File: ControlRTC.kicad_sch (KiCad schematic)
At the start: 40 parts, among them M1 Fan_4pin, SW1 SW_USER, SW2 SW_WIPE, U18 74LVC1G07, U19 74LVC1G07, U20 LP5569RTWR, U21 PCF85063AT, U25 PCF8563TS, U27 74LVC1G07, Y2 32768Hz{slash}12.5pF

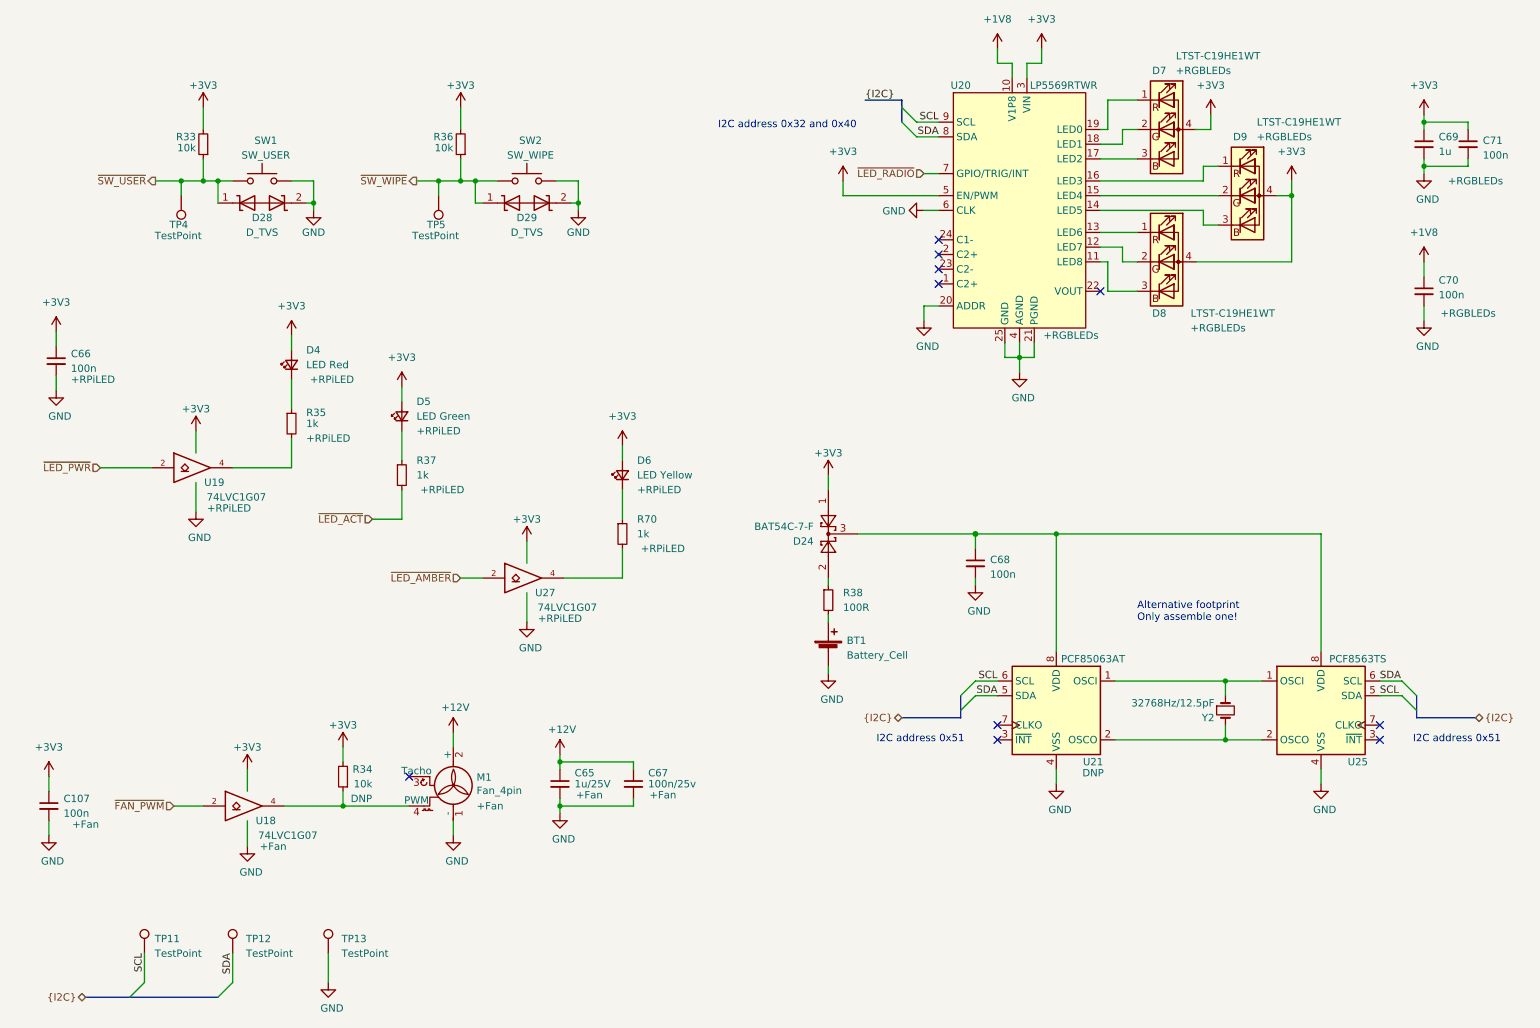
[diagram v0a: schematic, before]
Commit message: Yellow Proto1
Changes:
-name changed to yellow
-moved to 24-pin CP2102N
-routing

Signed-off-by: Dominik Sliwa <dominik@sliwa.io>
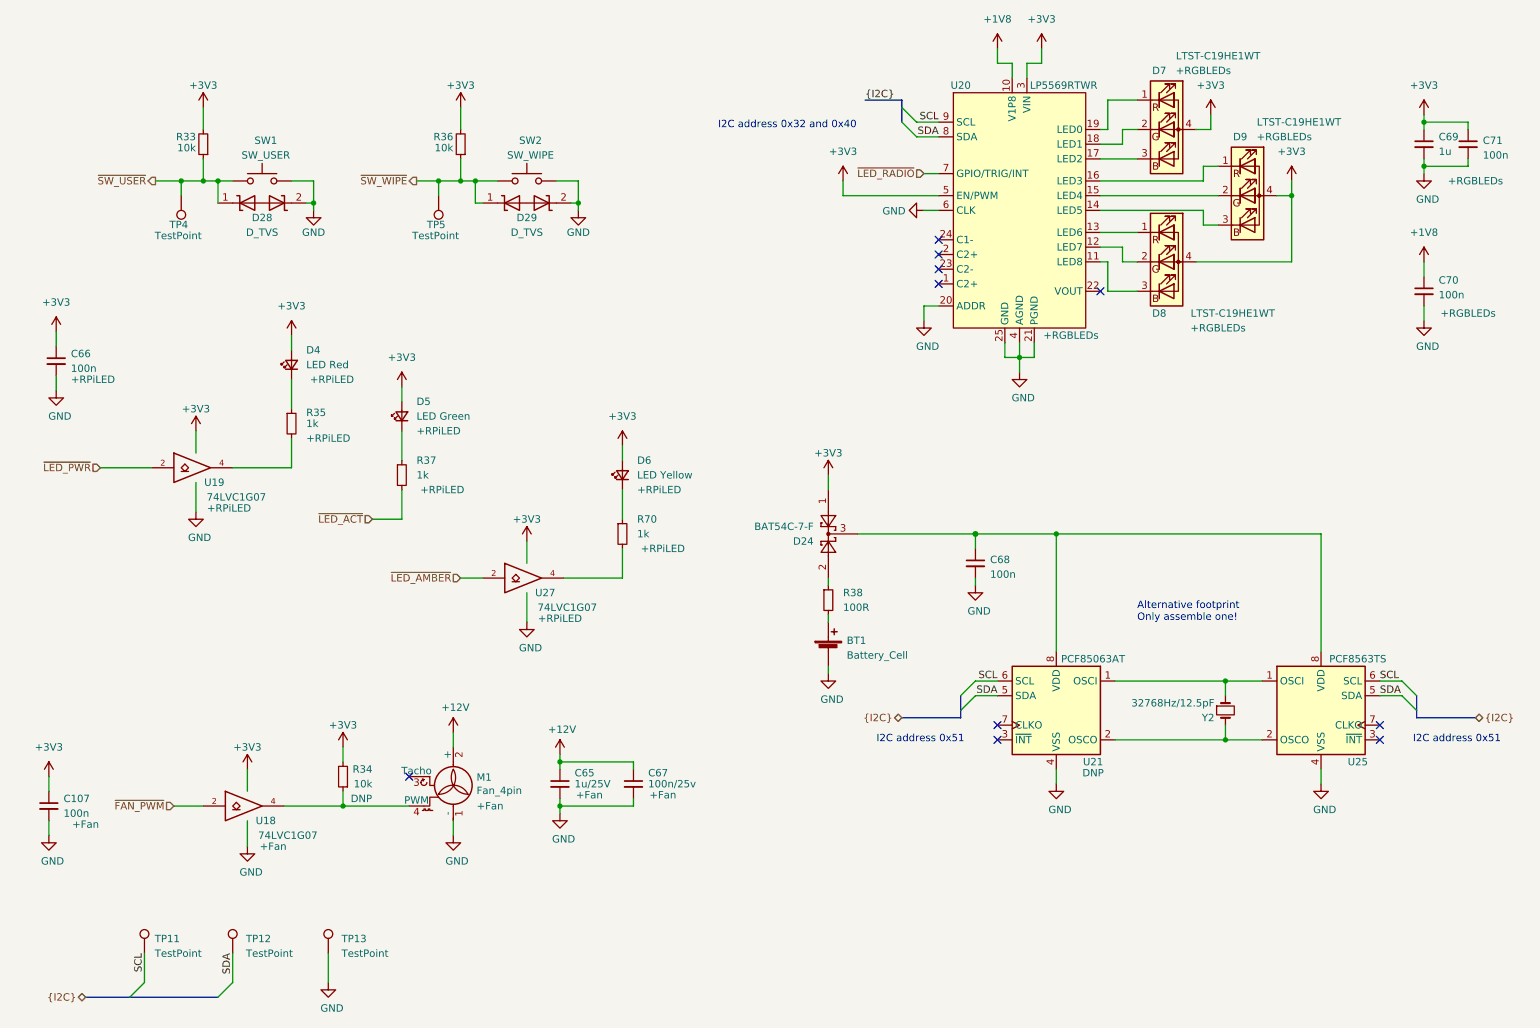
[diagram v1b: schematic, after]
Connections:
- net SCL: now also U25.6 (SCL); no longer U25.5 (SDA)
- net SDA: now also U25.5 (SDA); no longer U25.6 (SCL)

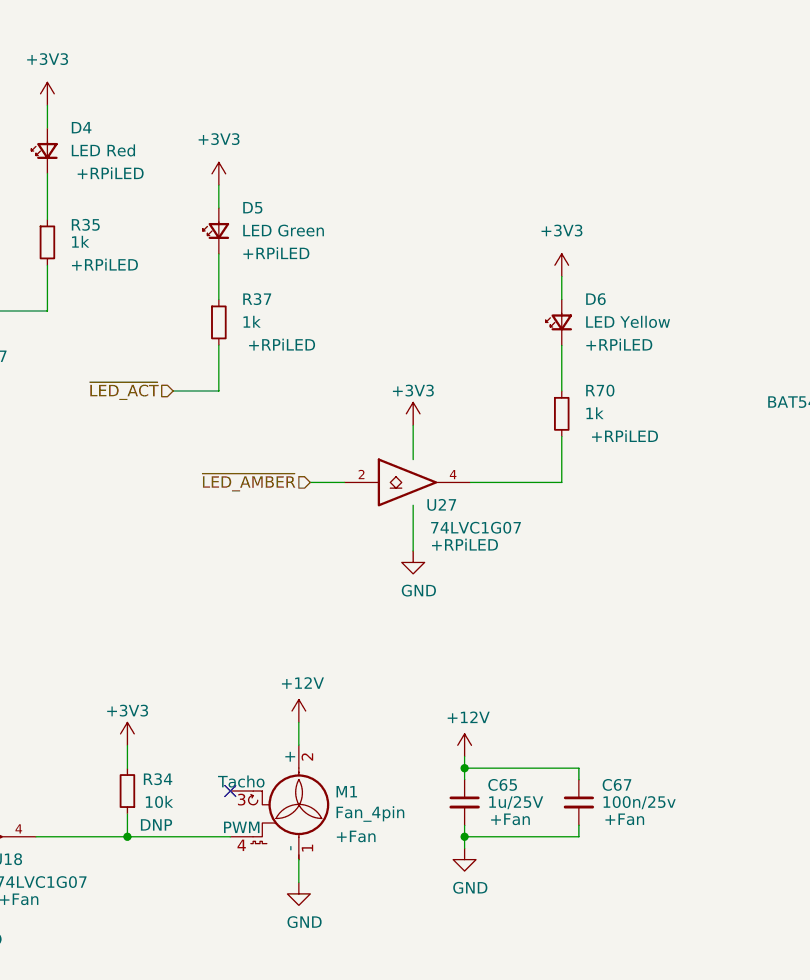
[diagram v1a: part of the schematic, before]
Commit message: Fix FSUSB30 Symbol and routing
Additionally a cap was added to U27.

Signed-off-by: Dominik Sliwa <dominik@sliwa.io>
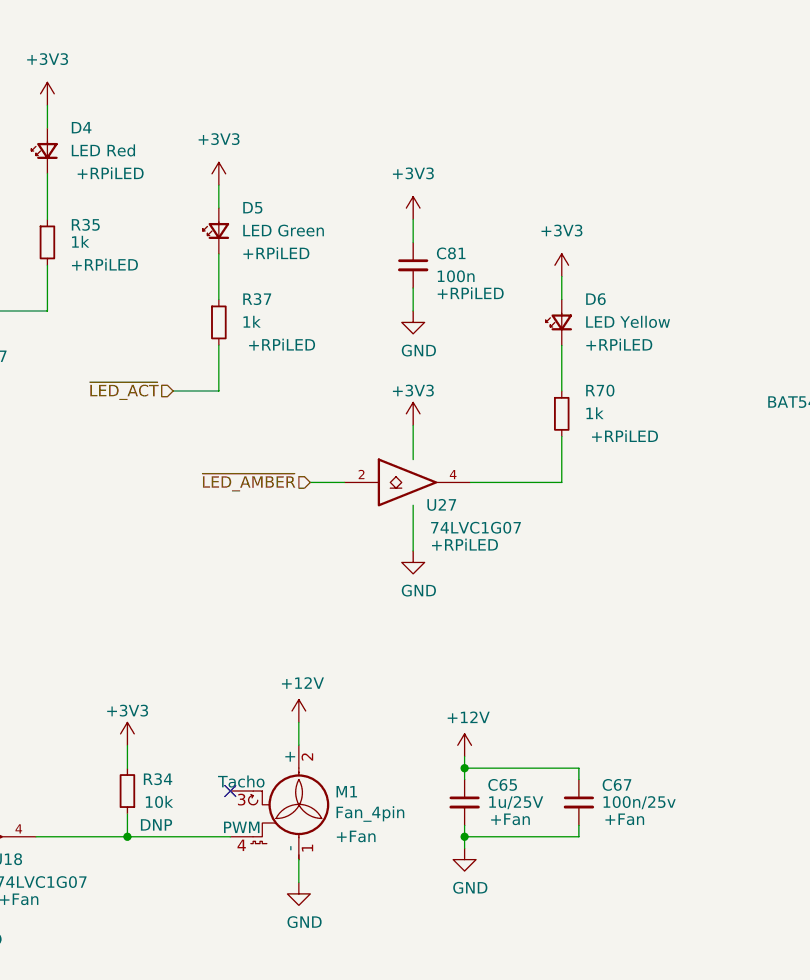
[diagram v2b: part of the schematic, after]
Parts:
- added C81: 100n, Capacitor_SMD:C_0402_1005Metric, symbol Device:C_Small
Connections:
- net +3V3: now also C81.1
- net GND: now also C81.2
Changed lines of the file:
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@@
-(kicad_sch (version 20210621) (generator eeschema)
+(kicad_sch (version 20211123) (generator eeschema)
   (paper "A4")
   (title_block
@@
     (comment 2 "Yellow")
   )
-  (junction (at 95.25 45.72) (diameter 0.9144) (color 0 0 0 0))
-  (junction (at 227.33 132.08) (diameter 0.9144) (color 0 0 0 0))
-  (junction (at 115.57 49.53) (diameter 0.9144) (color 0 0 0 0))
-  (junction (at 97.79 45.72) (diameter 0.9144) (color 0 0 0 0))
-  (junction (at 74.93 153.67) (diameter 0.9144) (color 0 0 0 0))
-  (junction (at 69.85 49.53) (diameter 0.9144) (color 0 0 0 0))
-  (junction (at 53.34 45.72) (diameter 0.9144) (color 0 0 0 0))
-  (junction (at 112.395 146.05) (diameter 0.9144) (color 0 0 0 0))
-  (junction (at 184.15 106.68) (diameter 1.016) (color 0 0 0 0))
-  (junction (at 227.33 142.24) (diameter 0.9144) (color 0 0 0 0))
-  (junction (at 112.395 153.67) (diameter 0.9144) (color 0 0 0 0))
-  (junction (at 261.62 43.18) (diameter 0.9144) (color 0 0 0 0))
-  (junction (at 261.62 35.56) (diameter 0.9144) (color 0 0 0 0))
-  (junction (at 198.12 106.68) (diameter 0.9144) (color 0 0 0 0))
-  (junction (at 91.44 45.72) (diameter 0.9144) (color 0 0 0 0))
-  (junction (at 191.77 76.2) (diameter 0.9144) (color 0 0 0 0))
-  (junction (at 46.99 45.72) (diameter 0.9144) (color 0 0 0 0))
-  (junction (at 238.76 48.26) (diameter 0.9144) (color 0 0 0 0))
-  (junction (at 50.8 45.72) (diameter 0.9144) (color 0 0 0 0))
+  (junction (at 112.395 146.05) (diameter 0.9144) (color 0 0 0 0)
+  )
+  (junction (at 261.62 35.56) (diameter 0.9144) (color 0 0 0 0)
+  )
+  (junction (at 184.15 106.68) (diameter 1.016) (color 0 0 0 0)
+  )
+  (junction (at 53.34 45.72) (diameter 0.9144) (color 0 0 0 0)
+  )
+  (junction (at 74.93 153.67) (diameter 0.9144) (color 0 0 0 0)
+  )
+  (junction (at 261.62 43.18) (diameter 0.9144) (color 0 0 0 0)
+  )
+  (junction (at 191.77 76.2) (diameter 0.9144) (color 0 0 0 0)
+  )
+  (junction (at 95.25 45.72) (diameter 0.9144) (color 0 0 0 0)
+  )
+  (junction (at 238.76 48.26) (diameter 0.9144) (color 0 0 0 0)
+  )
+  (junction (at 115.57 49.53) (diameter 0.9144) (color 0 0 0 0)
+  )
+  (junction (at 227.33 132.08) (diameter 0.9144) (color 0 0 0 0)
+  )
+  (junction (at 91.44 45.72) (diameter 0.9144) (color 0 0 0 0)
+  )
+  (junction (at 69.85 49.53) (diameter 0.9144) (color 0 0 0 0)
+  )
+  (junction (at 97.79 45.72) (diameter 0.9144) (color 0 0 0 0)
+  )
+  (junction (at 46.99 45.72) (diameter 0.9144) (color 0 0 0 0)
+  )
+  (junction (at 50.8 45.72) (diameter 0.9144) (color 0 0 0 0)
+  )
+  (junction (at 227.33 142.24) (diameter 0.9144) (color 0 0 0 0)
+  )
+  (junction (at 198.12 106.68) (diameter 0.9144) (color 0 0 0 0)
+  )
+  (junction (at 112.395 153.67) (diameter 0.9144) (color 0 0 0 0)
+  )
   (no_connect (at 177.8 58.42))
   (no_connect (at 86.36 148.59))
@@
     (stroke (width 0) (type solid) (color 0 0 0 0))
   )
+  (wire (pts (xy 106.68 92.71) (xy 106.68 95.25))
+    (stroke (width 0) (type solid) (color 0 0 0 0))
+  )
   (wire (pts (xy 45.72 153.67) (xy 50.8 153.67))
     (stroke (width 0) (type solid) (color 0 0 0 0))
@@
   )
   (wire (pts (xy 222.25 36.83) (xy 224.79 36.83))
+    (stroke (width 0) (type solid) (color 0 0 0 0))
+  )
+  (wire (pts (xy 106.68 85.09) (xy 106.68 87.63))
     (stroke (width 0) (type solid) (color 0 0 0 0))
   )
@@
     (pin "8")
   )
+  (symbol (lib_id "power:+3V3") (at 106.68 85.09 0) (unit 1)
+    (in_bom yes) (on_board yes)
+    (property "Reference" "#PWR0167" (id 0) (at 106.68 88.9 0)
+      (effects (font (size 1.27 1.27)) hide)
+    )
+    (property "Value" "+3V3" (id 1) (at 106.68 80.01 0))
+    (property "Footprint" "" (id 2) (at 106.68 85.09 0)
+      (effects (font (size 1.27 1.27)) hide)
+    )
+    (property "Datasheet" "" (id 3) (at 106.68 85.09 0)
+      (effects (font (size 1.27 1.27)) hide)
+    )
+    (pin "1")
+  )
   (symbol (lib_id "Device:LED_Small") (at 123.19 96.52 90) (unit 1)
     (in_bom yes) (on_board yes)
@@
     (pin "2")
   )
+  (symbol (lib_id "Device:C_Small") (at 106.68 90.17 0) (unit 1)
+    (in_bom yes) (on_board yes)
+    (property "Reference" "C81" (id 0) (at 109.22 88.9 0)
+      (effects (font (size 1.27 1.27)) (justify left))
+    )
+    (property "Value" "100n" (id 1) (at 109.22 91.44 0)
+      (effects (font (size 1.27 1.27)) (justify left))
+    )
+    (property "Footprint" "Capacitor_SMD:C_0402_1005Metric" (id 2) (at 106.68 90.17 0)
+      (effects (font (size 1.27 1.27)) hide)
+    )
+    (property "Datasheet" "~" (id 3) (at 106.68 90.17 0)
+      (effects (font (size 1.27 1.27)) hide)
+    )
+    (property "Config" "+RPiLED" (id 4) (at 113.03 93.345 0))
+    (pin "1")
+    (pin "2")
+  )
   (symbol (lib_id "Amber:D_TVS_Reverse") (at 60.96 49.53 0) (unit 1)
     (in_bom yes) (on_board yes)
@@
       (effects (font (size 1.27 1.27)) hide)
     )
+    (pin "1")
+  )
+  (symbol (lib_id "power:GND") (at 106.68 95.25 0) (unit 1)
+    (in_bom yes) (on_board yes)
+    (property "Reference" "#PWR0168" (id 0) (at 106.68 101.6 0)
+      (effects (font (size 1.27 1.27)) hide)
+    )
+    (property "Value" "GND" (id 1) (at 107.315 99.695 0))
+    (property "Footprint" "" (id 2) (at 106.68 95.25 0)
+      (effects (font (size 1.27 1.27)) hide)
+    )
+    (property "Datasheet" "" (id 3) (at 106.68 95.25 0)
+      (effects (font (size 1.27 1.27)) hide)
+    )

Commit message: Rename Amber to Yellow everywhere
Signed-off-by: Stefan Agner <stefan@agner.ch>
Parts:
- D28, D29: symbol Amber:D_TVS_Reverse -> Yellow:D_TVS_Reverse
- U20: symbol Amber:LP5569 -> Yellow:LP5569
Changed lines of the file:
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@@
     (pin "1")
   )
-  (symbol (lib_id "Amber:D_TVS_Reverse") (at 106.68 49.53 0) (unit 1)
+  (symbol (lib_id "Yellow:D_TVS_Reverse") (at 106.68 49.53 0) (unit 1)
     (in_bom yes) (on_board yes)
     (property "Reference" "D29" (id 0) (at 106.68 52.07 0))
@@
     (pin "2")
   )
-  (symbol (lib_id "Amber:D_TVS_Reverse") (at 60.96 49.53 0) (unit 1)
+  (symbol (lib_id "Yellow:D_TVS_Reverse") (at 60.96 49.53 0) (unit 1)
     (in_bom yes) (on_board yes)
     (property "Reference" "D28" (id 0) (at 60.96 52.07 0))
@@
     (pin "4")
   )
-  (symbol (lib_id "Amber:LP5569") (at 191.77 50.8 0) (unit 1)
+  (symbol (lib_id "Yellow:LP5569") (at 191.77 50.8 0) (unit 1)
     (in_bom yes) (on_board yes)
     (property "Reference" "U20" (id 0) (at 181.61 29.21 0))

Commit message: Exclude TestPoints from BOM
Signed-off-by: Stefan Agner <stefan@agner.ch>
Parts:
- TP11, TP12, TP13, TP4, TP5: now left out of the parts list
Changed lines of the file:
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@@
   )
   (symbol (lib_id "Connector:TestPoint") (at 72.39 179.07 0) (unit 1)
-    (in_bom yes) (on_board yes) (fields_autoplaced)
+    (in_bom no) (on_board yes) (fields_autoplaced)
     (property "Reference" "TP13" (id 0) (at 74.676 176.5934 0)
       (effects (font (size 1.27 1.27)) (justify left))
@@
   )
   (symbol (lib_id "Connector:TestPoint") (at 55.88 179.07 0) (unit 1)
-    (in_bom yes) (on_board yes) (fields_autoplaced)
+    (in_bom no) (on_board yes) (fields_autoplaced)
     (property "Reference" "TP12" (id 0) (at 58.166 176.5934 0)
       (effects (font (size 1.27 1.27)) (justify left))
@@
   )
   (symbol (lib_id "Connector:TestPoint") (at 40.64 179.07 0) (unit 1)
-    (in_bom yes) (on_board yes) (fields_autoplaced)
+    (in_bom no) (on_board yes) (fields_autoplaced)
     (property "Reference" "TP11" (id 0) (at 42.418 176.5934 0)
       (effects (font (size 1.27 1.27)) (justify left))
@@
   )
   (symbol (lib_id "Connector:TestPoint") (at 91.44 48.26 180) (unit 1)
-    (in_bom yes) (on_board yes)
+    (in_bom no) (on_board yes)
     (property "Reference" "TP5" (id 0) (at 89.408 53.2764 0)
       (effects (font (size 1.27 1.27)) (justify right))
@@
   )
   (symbol (lib_id "Connector:TestPoint") (at 46.99 48.26 180) (unit 1)
-    (in_bom yes) (on_board yes)
+    (in_bom no) (on_board yes)
     (property "Reference" "TP4" (id 0) (at 44.958 53.2764 0)
       (effects (font (size 1.27 1.27)) (justify right))

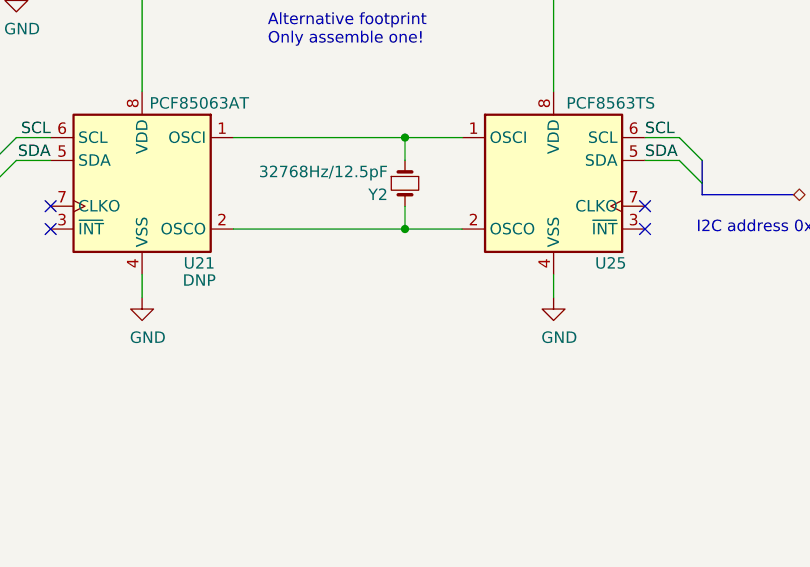
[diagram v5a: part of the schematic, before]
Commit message: Silkscreen fixes/small BOM adjustments
- Update silk screen reference designators
- Update backside silk screen for Yellow revision 1.1
- Set U21 (SOIC-8 RTC) to assemble and U25 (MSOP-8) as DNP
- Update heatsink footprint to add heatsink outline to silk screen (#44)
- Mark orientation of D26, D27, D28 and D29 (fixes #39)
- Use pin-header footprint for PoE selector J13, it is now JP5

Signed-off-by: Stefan Agner <stefan@agner.ch>
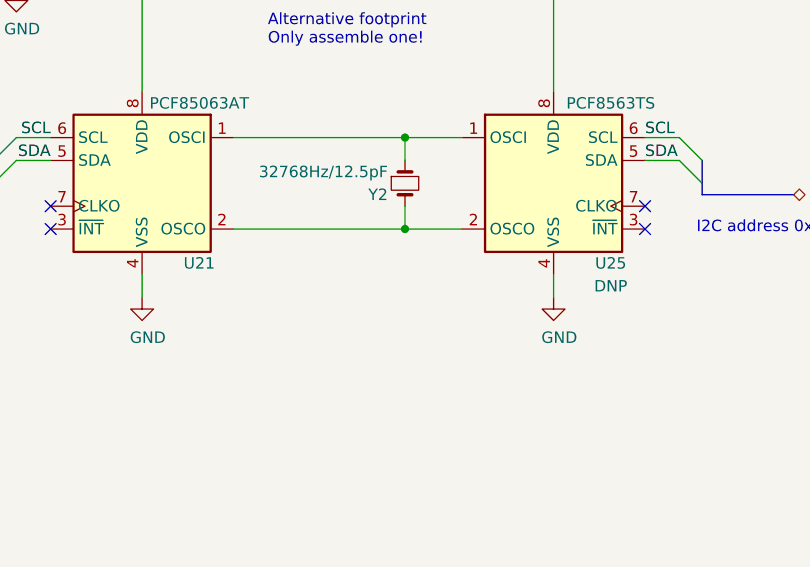
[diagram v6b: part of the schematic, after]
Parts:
- U21: Config DNP -> (none)
- U25: Config (none) -> DNP
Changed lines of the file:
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@@
   (title_block
     (title "Control/RTC")
-    (date "2021-08-30")
-    (rev "proto1")
+    (date "2022-01-08")
+    (rev "1.1")
     (company "Nabu Casa")
     (comment 1 "www.nabucasa.com")
@@
       (effects (font (size 1.27 1.27)) hide)
     )
-    (property "Config" "DNP" (id 6) (at 204.47 147.955 0))
     (pin "1")
     (pin "2")
@@
       (effects (font (size 1.27 1.27)) hide)
     )
-    (pin "1")
-    (pin "2")
+    (property "Config" "DNP" (id 6) (at 250.19 148.59 0))
+    (pin "1")
+    (pin "2")
